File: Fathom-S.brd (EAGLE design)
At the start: 112.4 x 45.7 mm, 109 parts, among them IC1 LMH6643, IC2 LMH6643, IC3 ST490AB, IC4 ST490AB, IC5 FT230XS, Q1 BC817-40W, U1 MC7812, U2 MC7805, U4 INA139, U5 MC7805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

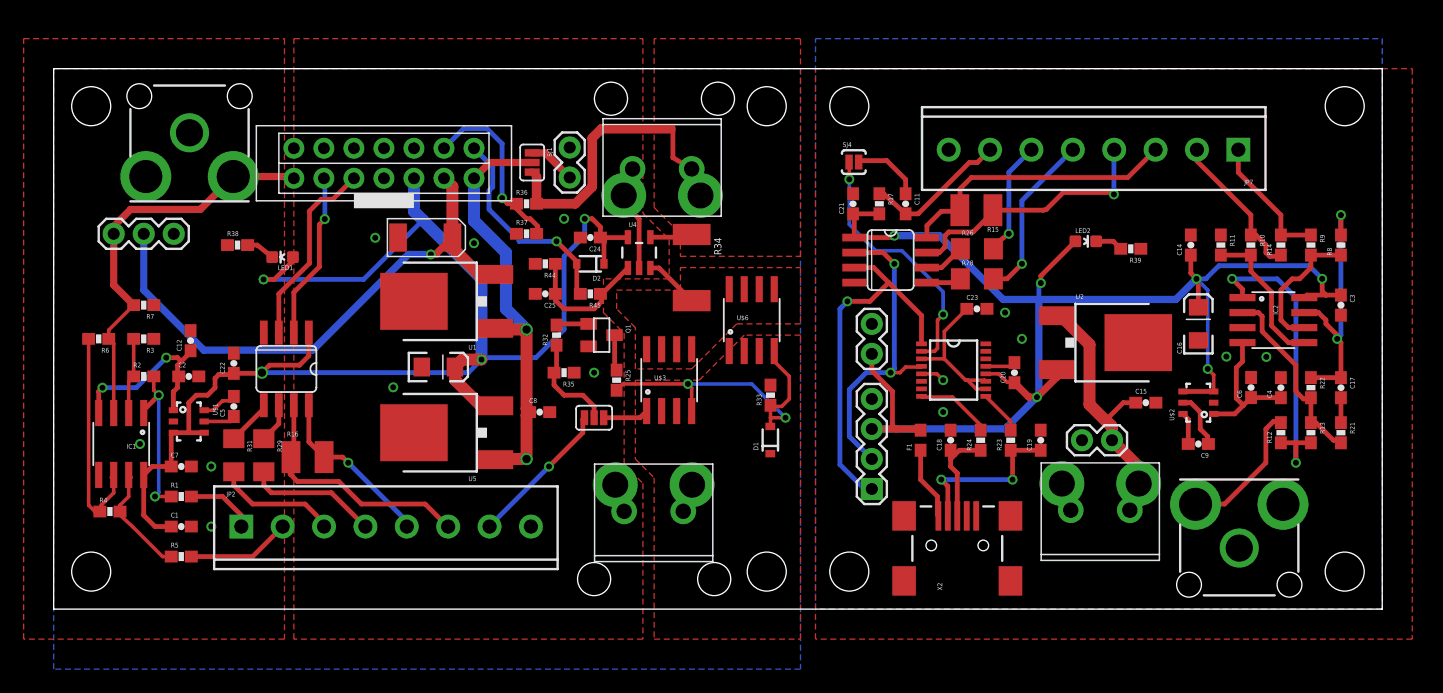
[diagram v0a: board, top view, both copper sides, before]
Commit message: Changed lm2776 components to match datasheet and hopefully fix our issues.
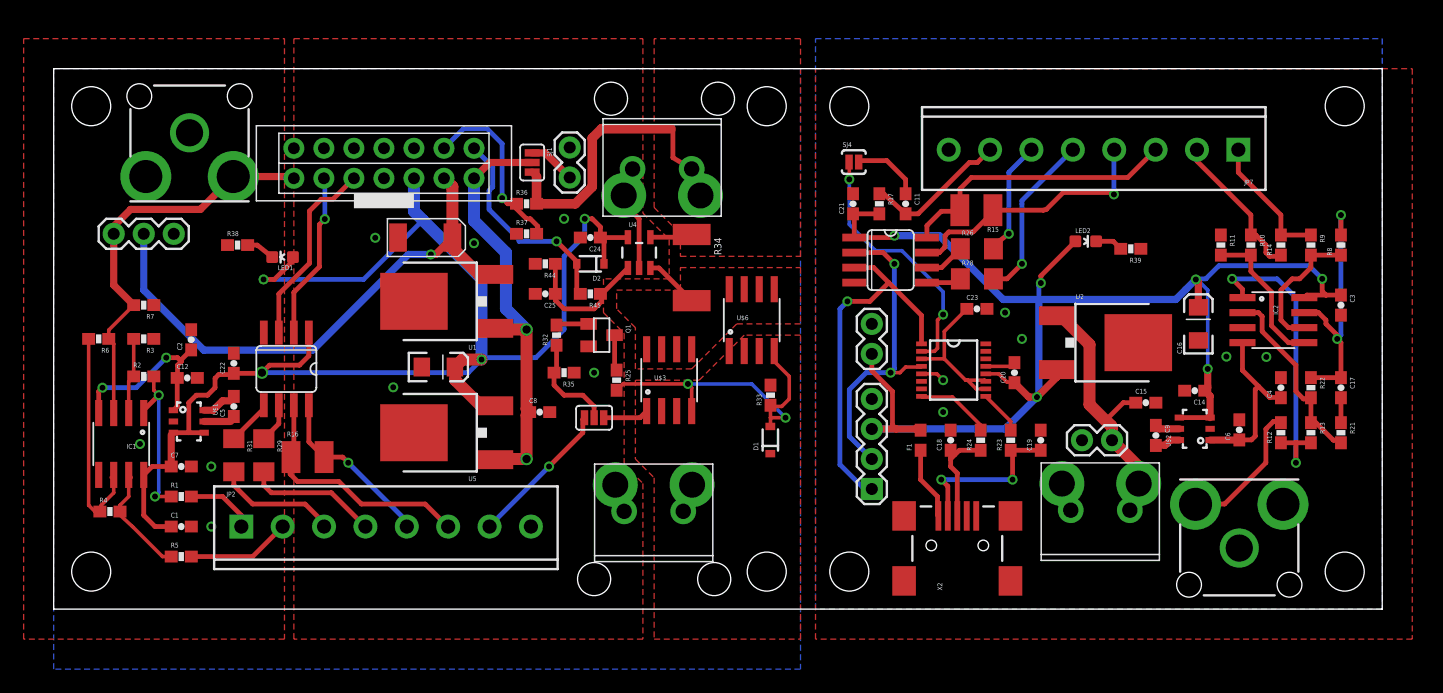
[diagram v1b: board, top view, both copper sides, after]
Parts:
- C12, C14, C6, C7: value 2.2uF X5R -> 10uF X5R 10V
- C5, C9: value 1uF X5R -> 1uF X5R 35V
- moved C14 12.3 mm to (96.5, 18.5), turned to 180 degrees
- moved C6 3.72 mm to (100.3, 15.2)
- moved C9 3.67 mm to (93.2, 14.7), turned to 270 degrees
- moved C12 3.16 mm to (11.3, 19.6), turned to 0 degrees
- moved C2 3.11 mm to (11.6, 22.8), turned to 90 degrees
- moved U$2 2.23 mm to (96.5, 15.3)
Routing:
- net -VCC: track 12.3 -> 15.1 mm
- net N$3: track 4.77 -> 2.11 mm
- net N$4: track 2.73 -> 2.18 mm

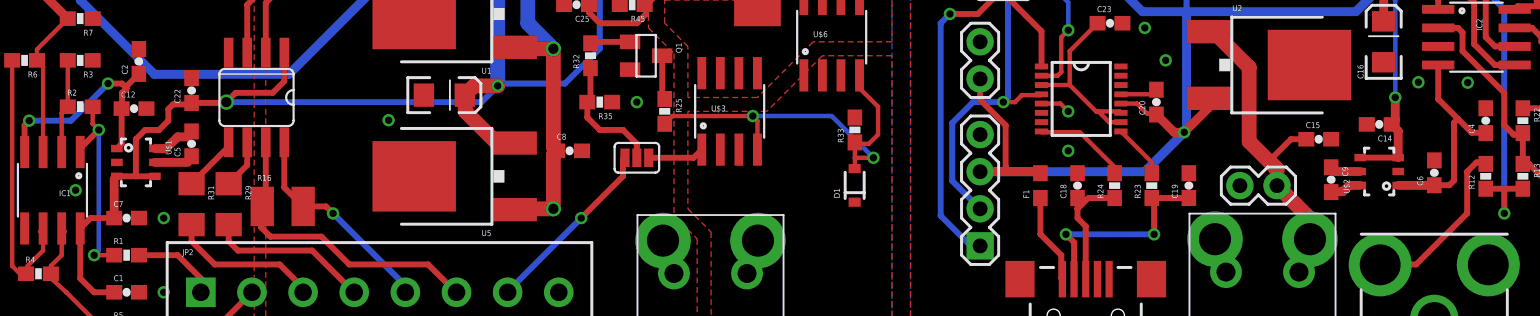
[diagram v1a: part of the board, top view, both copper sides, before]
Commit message: Layout 'typos' fixed.
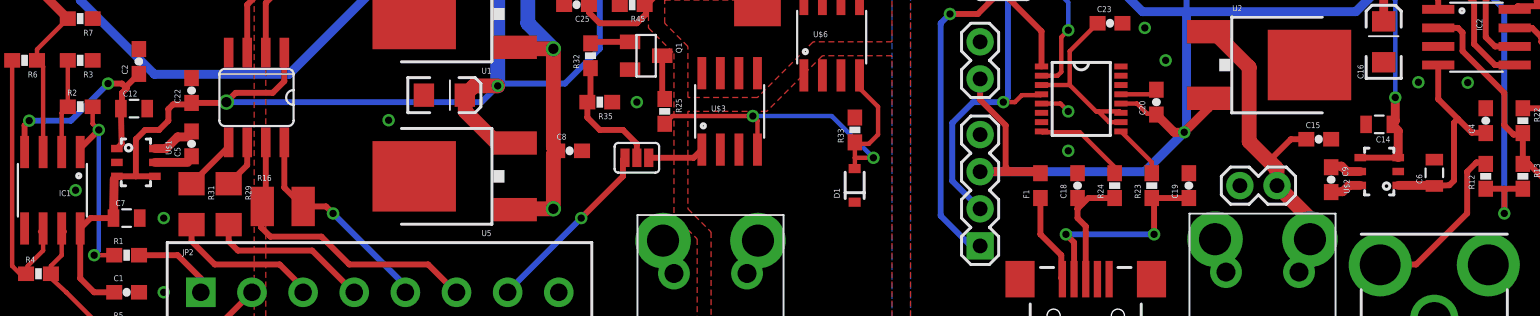
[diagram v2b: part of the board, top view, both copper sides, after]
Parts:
- C12, C14, C6, C7: device SparkFun-Passives:0603-CAP -> SparkFun-Passives:0805
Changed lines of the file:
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@@
 <element name="C1" library="SparkFun-Passives" package="0603-CAP" value="0.1uF" x="10.795" y="6.985"/>
 <element name="C10" library="SparkFun-Passives" package="EIA3216" value="10uF 16V" x="32.54375" y="20.47875" smashed="yes"/>
-<element name="C14" library="SparkFun-Passives" package="0603-CAP" value="10uF X5R 10V" x="96.5327" y="18.4785" rot="R180"/>
+<element name="C14" library="SparkFun-Passives" package="0805" value="10uF X5R 10V" x="96.5327" y="18.4785" rot="R180"/>
 <element name="C15" library="SparkFun-Passives" package="0603-CAP" value="0.1uF" x="92.3925" y="17.4625"/>
 <element name="C16" library="SparkFun-Passives" package="EIA3216" value="10uF 16V" x="96.8375" y="24.13" rot="R90"/>
@@
 <element name="C4" library="SparkFun-Passives" package="0603-CAP" value="0.1uF" x="103.8225" y="18.7325" rot="R90"/>
 <element name="C5" library="SparkFun-Passives" package="0603-CAP" value="1uF X5R 35V" x="15.24" y="17.145" rot="R90"/>
-<element name="C7" library="SparkFun-Passives" package="0603-CAP" value="10uF X5R 10V" x="10.795" y="12.065"/>
+<element name="C7" library="SparkFun-Passives" package="0805" value="10uF X5R 10V" x="10.795" y="12.065"/>
 <element name="C8" library="SparkFun-Passives" package="0603-CAP" value="0.1uF" x="41.11625" y="16.66875"/>
 <element name="C9" library="SparkFun-Passives" package="0603-CAP" value="1uF X5R 35V" x="93.2434" y="14.6939" rot="R270"/>
@@
 <attribute name="NAME" x="66.7385" y="39.0906" size="0.4064" layer="25"/>
 </element>
-<element name="C6" library="SparkFun-Passives" package="0603-CAP" value="10uF X5R 10V" x="100.3046" y="15.1638" rot="R90"/>
-<element name="C12" library="SparkFun-Passives" package="0603-CAP" value="10uF X5R 10V" x="11.303" y="19.558"/>
+<element name="C6" library="SparkFun-Passives" package="0805" value="10uF X5R 10V" x="100.3046" y="15.1638" rot="R90"/>
+<element name="C12" library="SparkFun-Passives" package="0805" value="10uF X5R 10V" x="11.303" y="19.558"/>
 </elements>
 <signals>
@@
 <wire x1="83.5152" y1="28.1947" x2="86.4355" y2="31.115" width="0.4064" layer="1"/>
 <wire x1="97.8327" y1="16.2027" x2="97.8327" y2="18.0285" width="0.6096" layer="1"/>
-<wire x1="97.8327" y1="18.0285" x2="97.3827" y2="18.4785" width="0.6096" layer="1"/>
+<wire x1="97.8327" y1="18.0285" x2="97.4327" y2="18.4785" width="0.6096" layer="1"/>
 <wire x1="97.63125" y1="20.32" x2="97.63125" y2="18.72705" width="0.6096" layer="1"/>
-<wire x1="97.63125" y1="18.72705" x2="97.3827" y2="18.4785" width="0.6096" layer="1"/>
+<wire x1="97.63125" y1="18.72705" x2="97.4327" y2="18.4785" width="0.6096" layer="1"/>
 <wire x1="96.8375" y1="25.53" x2="96.8375" y2="27.6733" width="0.6096" layer="1"/>
 <wire x1="96.8375" y1="27.6733" x2="96.624775" y2="27.886025" width="0.6096" layer="1"/>
@@
 <wire x1="10.795" y1="21.0956" x2="11.6332" y2="21.9338" width="0.4064" layer="1"/>
 <wire x1="10.4775" y1="20.6375" x2="10.4775" y2="19.5825" width="0.4064" layer="1"/>
-<wire x1="10.4775" y1="19.5825" x2="10.453" y2="19.558" width="0.4064" layer="1"/>
-<wire x1="10.453" y1="19.558" x2="10.453" y2="17.148" width="0.4064" layer="1"/>
+<wire x1="10.4775" y1="19.5825" x2="10.403" y2="19.558" width="0.4064" layer="1"/>
+<wire x1="10.403" y1="19.558" x2="10.453" y2="17.148" width="0.4064" layer="1"/>
 <wire x1="10.453" y1="17.148" x2="10.13" y2="16.825" width="0.4064" layer="1"/>
 </signal>
@@
 <contactref element="U$2" pad="5"/>
 <contactref element="C9" pad="1"/>
-<wire x1="95.2327" y1="15.2527" x2="93.5346" y2="15.2527" width="0.6096" layer="1"/>
-<wire x1="93.5346" y1="15.2527" x2="93.2434" y2="15.5439" width="0.6096" layer="1"/>
+<wire x1="95.2327" y1="15.2527" x2="94.3229" y2="15.2527" width="0.6096" layer="1"/>
+<wire x1="94.3229" y1="15.2527" x2="93.9546" y2="15.621" width="0.6096" layer="1"/>
+<wire x1="93.9546" y1="15.621" x2="93.2705" y2="15.621" width="0.6096" layer="1"/>
+<wire x1="93.2705" y1="15.621" x2="93.2434" y2="15.5439" width="0.6096" layer="1"/>
 </signal>
 <signal name="N$4">
@@
 <wire x1="8.5725" y1="6.985" x2="7.62" y2="7.9375" width="0.4064" layer="1"/>
 <wire x1="7.62" y1="7.9375" x2="7.62" y2="11.3538" width="0.4064" layer="1"/>
-<wire x1="9.945" y1="12.065" x2="9.945" y2="14.74" width="0.6096" layer="1"/>
+<wire x1="9.895" y1="12.065" x2="9.945" y2="14.74" width="0.6096" layer="1"/>
 <wire x1="9.945" y1="14.74" x2="10.13" y2="14.925" width="0.3048" layer="1"/>
-<wire x1="9.945" y1="12.065" x2="8.3312" y2="12.065" width="0.4064" layer="1"/>
+<wire x1="9.895" y1="12.065" x2="8.3312" y2="12.065" width="0.4064" layer="1"/>
 <wire x1="8.3312" y1="12.065" x2="7.62" y2="11.3538" width="0.4064" layer="1"/>
 <wire x1="10.13" y1="14.925" x2="11.43" y2="14.925" width="0.4064" layer="1"/>
@@
 <wire x1="102.87" y1="17.907" x2="103.798" y2="17.907" width="0.4064" layer="1"/>
 <wire x1="103.798" y1="17.907" x2="103.8225" y2="17.8825" width="0.4064" layer="1"/>
-<wire x1="100.3046" y1="14.3138" x2="101.3342" y2="14.3138" width="0.4064" layer="1"/>
+<wire x1="100.3046" y1="14.2638" x2="101.3342" y2="14.3138" width="0.4064" layer="1"/>
 <wire x1="101.3342" y1="14.3138" x2="101.6508" y2="14.6304" width="0.4064" layer="1"/>
 <wire x1="101.6508" y1="14.6304" x2="101.6508" y2="18.5928" width="0.4064" layer="1"/>
 <wire x1="101.6508" y1="18.5928" x2="101.9175" y2="18.8595" width="0.4064" layer="1"/>
 <wire x1="97.8327" y1="14.3027" x2="100.2935" y2="14.3027" width="0.6096" layer="1"/>
-<wire x1="100.2935" y1="14.3027" x2="100.3046" y2="14.3138" width="0.6096" layer="1"/>
+<wire x1="100.2935" y1="14.3027" x2="100.3046" y2="14.2638" width="0.6096" layer="1"/>
 </signal>
 <signal name="N$24">

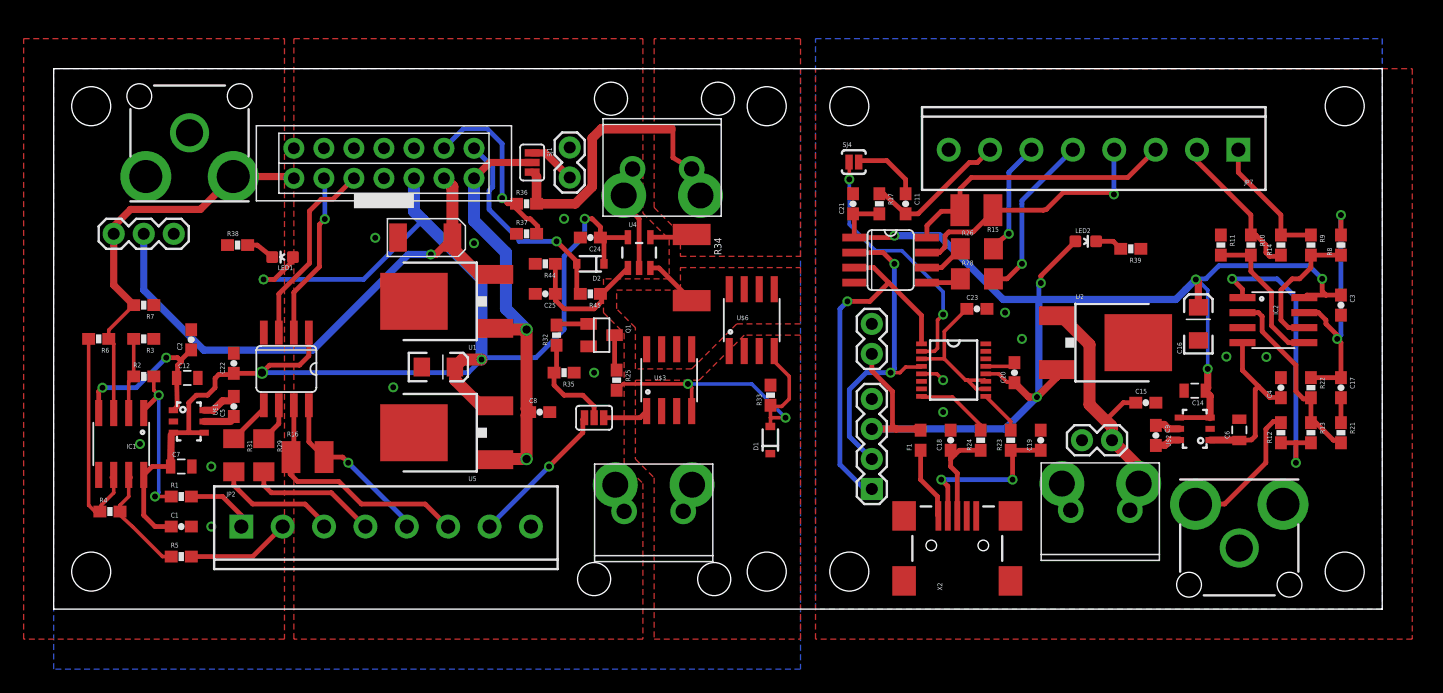
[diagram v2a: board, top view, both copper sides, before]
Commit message: Redid the layout for the video amplifiers and supply inverters to help fix recent issues. There is now an analog ground plane. LM2776 are laid out almost identical to the eval board.
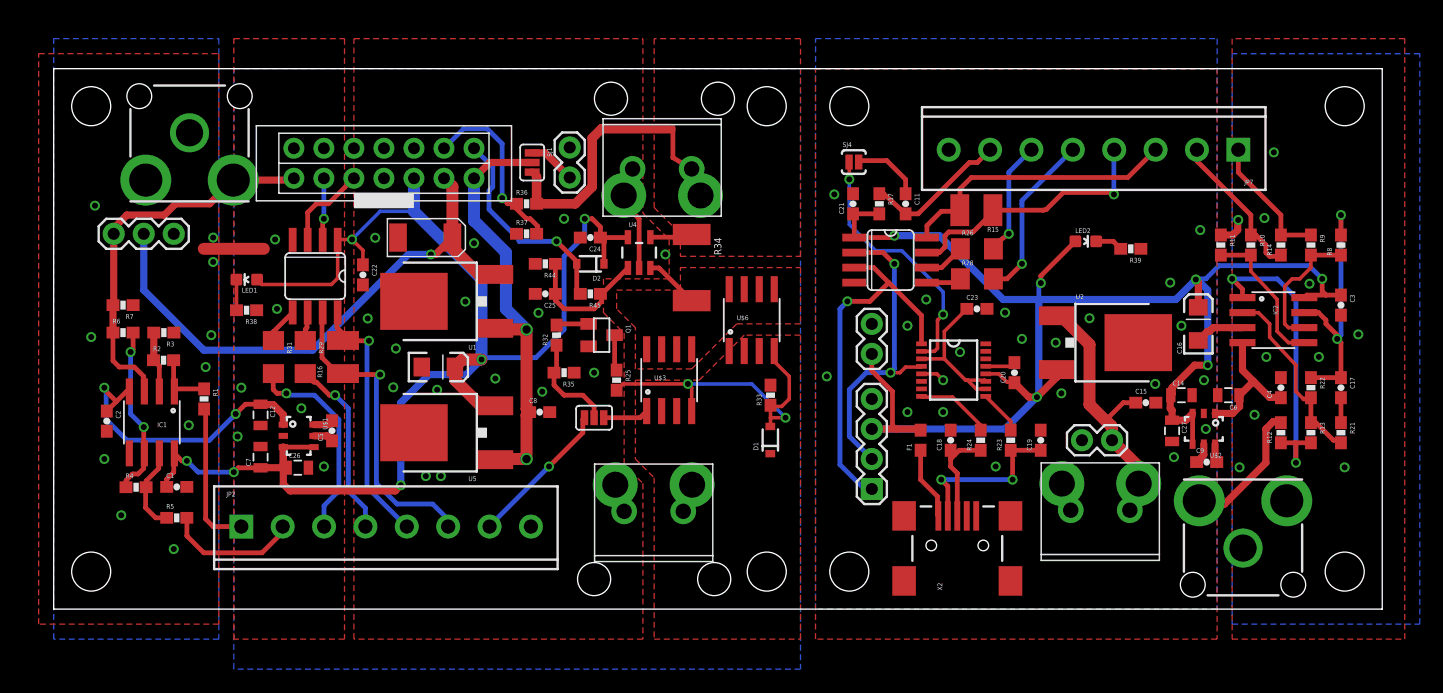
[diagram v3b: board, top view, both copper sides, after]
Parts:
- added C26, C27: 10uF X5R 10V, SparkFun-Passives:0805
- JP1, JP6: device BR-Eagle-Library:RCA -> BlueRobotics-Main:RCA
- moved C22 13.2 mm to (26.2, 28.3), turned to 270 degrees
- moved C2 9.92 mm to (4.50, 15.9), turned to 270 degrees
- moved U$1 9.38 mm to (20.7, 14.7)
- moved R29 9.02 mm to (21.3, 21.3)
- moved R16 8.98 mm to (24.5, 21.3), turned to 90 degrees
- moved R31 8.96 mm to (18.6, 21.3)
- moved C5 8.56 mm to (23.5, 15.1)
- moved R1 8.48 mm to (12.7, 17.8), turned to 270 degrees
- moved IC4 8.22 mm to (22.1, 28.2)
- moved C12 6.94 mm to (17.5, 16.4), turned to 270 degrees
- moved C7 6.75 mm to (17.5, 12.9), turned to 90 degrees
- moved R38 5.56 mm to (16.3, 25.3), turned to 180 degrees
- moved C9 4.85 mm to (97.5, 12.4), turned to 0 degrees
- moved LED1 3.58 mm to (16.3, 27.9)
- moved C1 3.37 mm to (10.4, 10.3)
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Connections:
- net GND: now also C27.2
- net GND-ISO: now also C26.2
- net VCC: now also C27.1
- net VCC-ISO: now also C26.1
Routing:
- net -VCC-ISO: track 15.9 -> 25.1 mm
- net ROV-RX: track 14.2 -> 5.25 mm
- net ROV-TX: track 16.3 -> 7.42 mm
- net N$1: track 13.9 -> 5.27 mm, vias 2 -> 0
- net ROV-TP3+: track 14.6 -> 22.0 mm
- net ROV-TP2+: track 10.4 -> 17.5 mm, vias 0 -> 1
- net ROV-TP1+: track 5.84 -> 12.6 mm
- net GND: track 4.61 -> 11.3 mm, vias 6 -> 31
- net GND-ISO: track 4.61 -> 9.69 mm, vias 8 -> 31
- net ROV-TP3-: track 21.6 -> 26.6 mm, vias 0 -> 1
- net N$6: track 19.1 -> 14.6 mm, vias 0 -> 2
- net ROV-TP2-: track 11.2 -> 15.5 mm, vias 0 -> 1
- net VCC: track 119.3 -> 123.3 mm
- net -VCC: track 15.1 -> 11.8 mm
- net N$2: track 10.0 -> 7.23 mm
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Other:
- board text added: "FATHOM-S ROV Board rev3"
- board text added: "FATHOM-S Topside Board rev3"
- board text removed: "FATHOM-ROV-INTERFACE rev2"
- board text removed: "FATHOM-TOPSIDE-INTERFACE rev2"

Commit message: Fixed a few minor ground issues.
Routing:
- net GND-ISO: vias 31 -> 35
- net GND: vias 31 -> 35
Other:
- board text added: "11/15"
- board text removed: "10/15"
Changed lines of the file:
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@@
 <text x="66.19875" y="24.13" size="0.8128" layer="51" ratio="12" align="center">GND</text>
 <text x="66.19875" y="21.59" size="0.8128" layer="51" ratio="12" align="center">+5V</text>
-<text x="65.405" y="26.035" size="0.8128" layer="51" ratio="12" rot="SR270" align="center-right">5V OUT</text>
+<text x="65.0875" y="25.87625" size="0.8128" layer="51" ratio="12" rot="SR270" align="center-right">5V OUT</text>
 <text x="107.315" y="12.54125" size="0.8128" layer="51" ratio="12" rot="R90" align="center-right">VIDEO OUT</text>
 <wire x1="89.05875" y1="32.385" x2="81.75625" y2="32.385" width="0.127" layer="51"/>
@@
 <text x="58.57875" y="36.83" size="0.8128" layer="51" ratio="12" distance="20" rot="R90" align="center">SWITCHED
 BATT PWR</text>
-<text x="2.69875" y="38.735" size="1.778" layer="52" rot="MR270">10/15</text>
-<text x="66.9925" y="38.735" size="1.778" layer="52" rot="MR270">10/15</text>
+<text x="2.69875" y="38.735" size="1.778" layer="52" rot="MR270">11/15</text>
+<text x="66.9925" y="38.735" size="1.778" layer="52" rot="MR270">11/15</text>
 <wire x1="63.8175" y1="45.72" x2="63.8175" y2="0" width="0.6096" layer="102"/>
 <text x="0.9525" y="5.3975" size="1.016" layer="52" ratio="12" rot="SMR90">*Only if VBAT&gt;13V</text>
@@
 <via x="84.7725" y="22.5425" extent="1-16" drill="0.5"/>
 <via x="87.63" y="24.60625" extent="1-16" drill="0.5"/>
+<via x="89.8525" y="27.6225" extent="1-16" drill="0.5"/>
+<via x="85.725" y="27.6225" extent="1-16" drill="0.5"/>
+<via x="82.07375" y="27.6225" extent="1-16" drill="0.5"/>
+<via x="66.04" y="26.82875" extent="1-16" drill="0.5"/>
 </signal>
 <signal name="N$10">
@@
 <contactref element="U5" pad="4"/>
 <contactref element="U1" pad="4"/>
-<polygon width="0.4064" layer="1" isolate="0.3048">
+<polygon width="0.4064" layer="1" isolate="0.254">
 <vertex x="15.24" y="-2.54"/>
 <vertex x="15.24" y="48.26"/>
-<vertex x="24.60625" y="48.26"/>
-<vertex x="24.60625" y="-2.54"/>
+<vertex x="25.4" y="48.26"/>
+<vertex x="25.4" y="-2.54"/>
 </polygon>
 <polygon width="0.4064" layer="16" isolate="0.3048">
@@
 <via x="34.8234" y="26.01595" extent="1-16" drill="0.5"/>
 <via x="51.7525" y="30.00375" extent="1-16" drill="0.5"/>
+<via x="17.4625" y="10.63625" extent="1-16" drill="0.5"/>
+<via x="21.11375" y="8.73125" extent="1-16" drill="0.5"/>
+<via x="18.0975" y="38.735" extent="1-16" drill="0.5"/>
+<via x="25.87625" y="33.49625" extent="1-16" drill="0.5"/>
 </signal>
 <signal name="VCC-ISO">
@@
 <wire x1="50.48" y1="31.4626" x2="53.7451" y2="31.4626" width="0.4064" layer="1"/>
 <wire x1="53.7451" y1="31.4626" x2="53.975" y2="31.6925" width="0.4064" layer="1"/>
-<polygon width="0.4064" layer="1" thermals="no">
+<polygon width="0.4064" layer="1" isolate="0.254" thermals="no">
 <vertex x="63.1825" y="29.845"/>
 <vertex x="63.1825" y="48.26"/>
